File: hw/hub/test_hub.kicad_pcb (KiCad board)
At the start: 2 copper layers, 88.9 x 76.2 mm, 108 parts, among them J1 ARM-SWD, P1 USB_OTG, P2 5V_SEL, P3 5V_EXT, P4 USB1, P5 USB2, P6 USB3, P7 UART, SW1 RST, SW2 BOOT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

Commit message: Update test_hub
No more rescued components
Ripped up all traces
Starting layout again
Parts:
- removed P1: USB_OTG, footprints:10118193-0001LF
- removed P4: USB1, footprints:292303-1
- removed P5: USB2, footprints:292303-1
- removed P6: USB3, footprints:292303-1
- removed R17, R20, R23: R_SNS, footprints:LVK12
- removed R18, R21, R24: 0, Resistors_SMD:R_0603
- removed R19, R22: 100, Resistors_SMD:R_0603
- removed R26, R27, R28: 1k, Resistors_SMD:R_0603
- removed U7, U8, U9: LT6106, footprints:TSOT-23-5
- added C35: 0.1uF, Capacitors_SMD:C_0603, F.Cu at (96.8, 186.3)
- added FB10: Ferrite_Bead, Resistors_SMD:R_0603, F.Cu at (182.0, 146.0)
- added FB7: Ferrite_Bead, Resistors_SMD:R_0603, F.Cu at (188.8, 118.9)
- added FB8: Ferrite_Bead, Resistors_SMD:R_0603, F.Cu at (188.6, 125.9)
- added FB9: Ferrite_Bead, Resistors_SMD:R_0603, F.Cu at (181.6, 138.8)
- added J2: USB_OTG, footprints:USB_MICRO_B, F.Cu at (54.7, 162.8)
- added J3: USB_OTG, footprints:USB_MICRO_B, F.Cu at (52.3, 139.9)
- added J4: USB_A, footprints:292303-1, F.Cu at (178.5, 160.4)
- added J5: USB_A, footprints:292303-1, F.Cu at (193.9, 122.3)
- added J6: USB_A, footprints:292303-1, F.Cu at (189.2, 141.9)
- D6: value LED2 -> LED3
- D7: value LED1 -> LED2
- D8: value LED0 -> LED1
- R16: value 100 -> 330
- moved FB3 103.6 mm to (53.2, 177.0)
- moved FB5 93.2 mm to (55.8, 126.2)
- moved FB4 92.1 mm to (57.4, 157.6)
- moved FB6 91.9 mm to (57.0, 133.4)
- moved C31 81.6 mm to (155.8, 87.0)
- moved D5 81.6 mm to (152.0, 76.9)
- moved R33 81.6 mm to (155.1, 76.9)
- moved U4 81.6 mm to (157.2, 81.4)
- moved C16 81.6 mm to (147.7, 81.6)
- moved C19 81.6 mm to (153.3, 81.4)
- moved C28 81.6 mm to (161.2, 79.0)
- moved R13 81.6 mm to (155.1, 78.9)
- moved U5 59.3 mm to (132.8, 79.8)
- moved C17 59.3 mm to (122.6, 79.7)
- moved C20 59.3 mm to (128.3, 79.8)
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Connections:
- net Net-(R11-Pad1) renamed /ST_USB_N
- net Net-(R12-Pad1) renamed /ST_USB_P
- C28 pad 2: Net-(C28-Pad2) -> /5V_OUT1
- C29 pad 2: Net-(C29-Pad2) -> /5V_OUT2
- C30 pad 2: Net-(C30-Pad2) -> /5V_OUT3
- C31 pad 1: Net-(C28-Pad2) -> /5V_OUT1
- C32 pad 1: Net-(C29-Pad2) -> /5V_OUT2
- C33 pad 1: Net-(C30-Pad2) -> /5V_OUT3
- FB3 pad 1: GND -> Net-(FB3-Pad1)
- FB3 pad 2: Net-(FB3-Pad2) -> +5V
- FB4 pad 1: /5V_OUT2 -> Net-(FB4-Pad1)
- FB4 pad 2: Net-(FB4-Pad2) -> GND
- FB5 pad 1: GND -> +5V
- FB6 pad 1: /5V_OUT3 -> GND
- R16 pad 1: Net-(R16-Pad1) -> GNDPWR
- R16 pad 2: Net-(R16-Pad2) -> GND
- R34 pad 2: /LED2 -> /LED3
- R35 pad 2: /LED1 -> /LED2
- R36 pad 2: /LED0 -> /LED1
- U3 pad 12: /SNS1 -> Net-(U3-Pad12)
- U3 pad 13: /SNS2 -> Net-(U3-Pad13)
- U3 pad 14: /SNS3 -> Net-(U3-Pad14)
- U3 pad 2: /LED0 -> /LED1
- U3 pad 3: /LED1 -> /LED2
- U3 pad 4: /LED2 -> /LED3
- U4 pad 1: Net-(C28-Pad2) -> /5V_OUT1
- U5 pad 1: Net-(C29-Pad2) -> /5V_OUT2
- U6 pad 1: Net-(C30-Pad2) -> /5V_OUT3
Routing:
- net /5V_OUT: track 293.7 -> 0.00 mm, vias 2 -> 0
- net +3V3: track 244.4 -> 0.00 mm, vias 19 -> 0
- net GND: track 218.5 -> 0.00 mm, vias 35 -> 0
- net GNDPWR: track 171.7 -> 0.00 mm, vias 1 -> 0
- net /5V_EN3: track 116.5 -> 0.00 mm, vias 2 -> 0
- net /SNS1: track 112.4 -> 0.00 mm, vias 4 -> 0
- net /5V_FLG3: track 109.3 -> 0.00 mm, vias 2 -> 0
- net /SNS2: track 107.2 -> 0.00 mm, vias 6 -> 0
- net /nRST: track 107.1 -> 0.00 mm, vias 6 -> 0
- net /SNS3: track 105.8 -> 0.00 mm, vias 2 -> 0
- net +5V: track 92.6 -> 0.00 mm, vias 2 -> 0
- net /BOOT0: track 75.9 -> 0.00 mm, vias 6 -> 0
- net /USB3_N: track 69.5 -> 0.00 mm
- net /USB3_P: track 69.3 -> 0.00 mm
- net /5V_FLG1: track 63.5 -> 0.00 mm, vias 2 -> 0
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- removed copper zone on B.Cu, net GND
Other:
- net class Default: clearance 0.16 -> 0.1524; trace_width 0.13 -> 0.1524; via_dia 0.6 -> 0.6858; via_drill 0.305 -> 0.3302
- rule trace_clearance: 0.16 -> 0.1524
- rule trace_min: 0.13 -> 0.1524
- rule via_min_drill: 0.305 -> 0.3302
- rule via_min_size: 0.6 -> 0.6858
- board text added: "USB Test Hub v0.2"
- board text removed: "USB Test Hub v0.1"

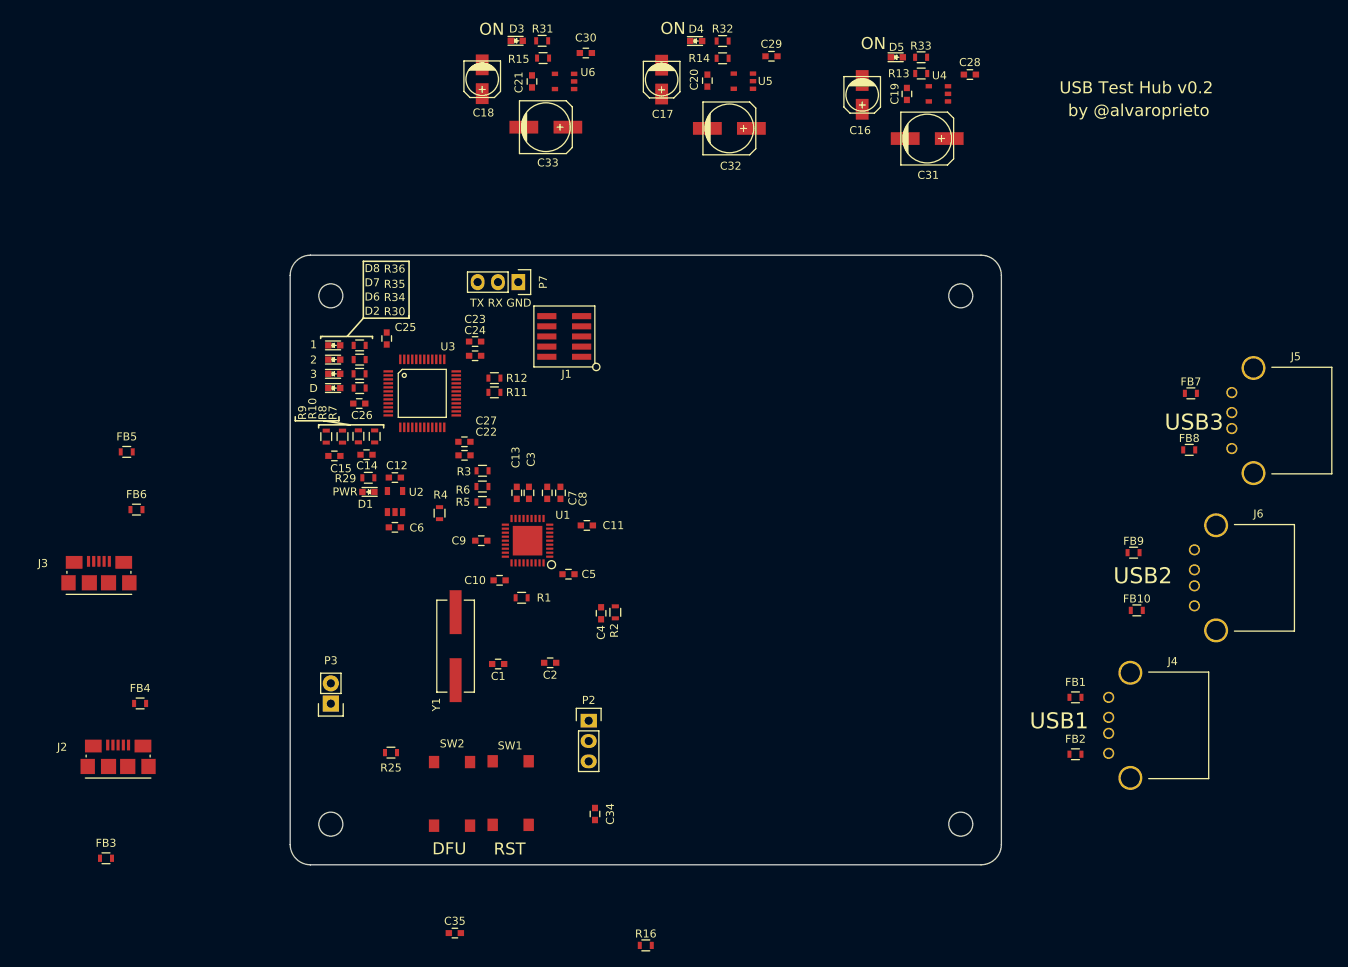
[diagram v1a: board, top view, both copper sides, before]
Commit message: More test_hub work
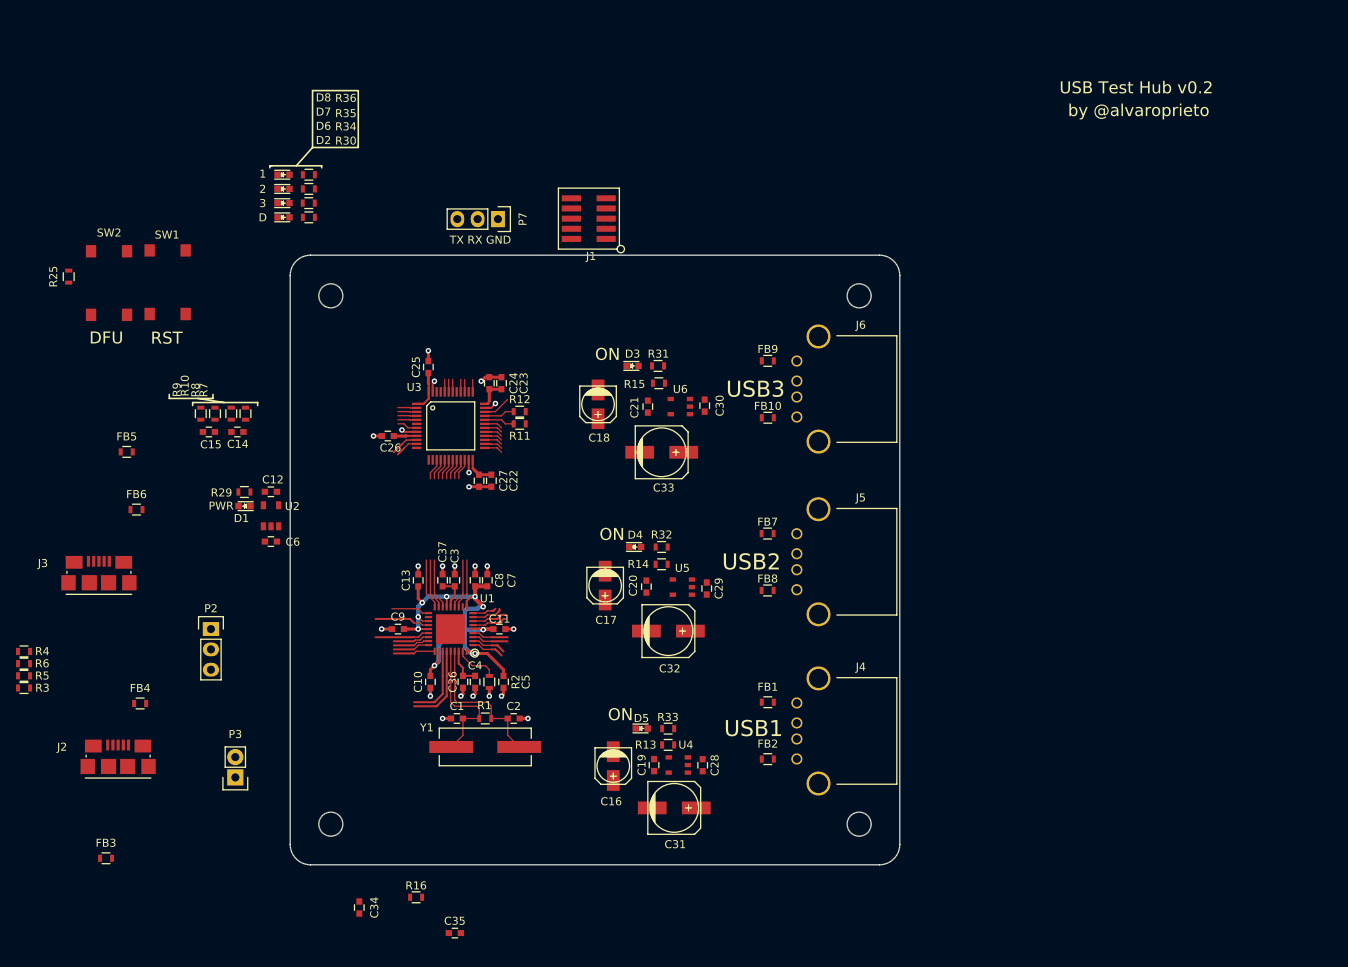
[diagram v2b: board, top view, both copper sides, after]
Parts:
- added C36: 1uF, Capacitors_SMD:C_0603, F.Cu at (97.8, 154.9)
- added C37: 1uF, Capacitors_SMD:C_0603, F.Cu at (95.2, 142.2)
- moved C28 92.6 mm to (127.8, 165.4), turned to 270 degrees
- moved U4 90.0 mm to (124.7, 165.3)
- moved D5 89.8 mm to (120.1, 160.8)
- moved R13 89.7 mm to (123.4, 162.8)
- moved R33 89.7 mm to (123.4, 160.8)
- moved C19 89.7 mm to (121.7, 165.3)
- moved C16 89.5 mm to (116.6, 165.5)
- moved C31 89.4 mm to (124.2, 170.7)
- moved SW1 76.9 mm to (60.9, 105.0)
- moved SW2 76.9 mm to (53.6, 105.1)
- moved R25 71.9 mm to (48.5, 104.3), turned to 90 degrees
- moved C29 67.0 mm to (128.3, 143.3), turned to 270 degrees
- moved U5 63.7 mm to (125.2, 143.1)
- moved C20 63.7 mm to (120.7, 143.0)
- moved D4 63.7 mm to (119.3, 138.1)
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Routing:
- net +3V3: track 0.00 -> 70.1 mm, vias 0 -> 9
- net GND: track 0.00 -> 29.4 mm, vias 0 -> 22
- net Net-(C2-Pad1): track 0.00 -> 18.7 mm
- net Net-(C1-Pad1): track 0.00 -> 17.7 mm
- net /USB_UP_P: track 0.00 -> 10.2 mm
- net /USB_UP_N: track 0.00 -> 9.34 mm
- net /PRTPWR3: track 0.00 -> 8.97 mm
- net /OCS_N2: track 0.00 -> 8.97 mm
- net /PRTPWR2: track 0.00 -> 8.96 mm
- net /OCS_N1: track 0.00 -> 8.95 mm
- net /PRTPWR1: track 0.00 -> 8.95 mm
- net /SDA: track 0.00 -> 8.53 mm
- net /SCL: track 0.00 -> 8.42 mm
- net /VBUS_DET: track 0.00 -> 8.07 mm
- net /OCS_N3: track 0.00 -> 7.50 mm
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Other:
- board size 88.9 x 76.2 mm -> 76.2 x 76.2 mm

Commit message: Continued routing work on test_hub
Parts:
- moved FB3 46.9 mm to (83.3, 141.1)
- moved FB5 41.2 mm to (83.1, 157.1)
- moved FB6 38.3 mm to (83.0, 161.4), turned to 180 degrees
- moved P2 37.6 mm to (100.6, 163.8)
- moved J3 34.2 mm to (80.3, 159.6), turned to 270 degrees
- moved J2 32.2 mm to (80.3, 143.2), turned to 270 degrees
- moved FB4 28.9 mm to (83.3, 144.8)
- moved R3 27.6 mm to (68.2, 144.5)
- moved R4 27.6 mm to (68.2, 140.0)
- moved R5 27.6 mm to (68.2, 143.0)
- moved R6 27.6 mm to (68.2, 141.5)
- moved D2 23.1 mm to (81.7, 119.1)
- moved D7 23.1 mm to (81.7, 115.5)
- moved R30 23.1 mm to (84.9, 119.1)
- moved R35 23.1 mm to (84.9, 115.5)
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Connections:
- FB5 pad 1: +5V -> Net-(FB5-Pad1)
- FB5 pad 2: Net-(FB5-Pad2) -> /5V_EXT
- J3 pad 1: Net-(FB5-Pad2) -> Net-(FB5-Pad1)
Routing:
- net /5V_OUT: track 0.00 -> 192.8 mm, vias 0 -> 3
- net /USB3_N: track 4.40 -> 73.4 mm
- net /USB3_P: track 4.41 -> 73.3 mm
- net GND: track 29.4 -> 86.5 mm, vias 22 -> 37
- net /USB2_N: track 4.55 -> 59.6 mm
- net /USB2_P: track 4.55 -> 59.5 mm
- net /USB1_N: track 4.47 -> 50.2 mm
- net /USB1_P: track 4.36 -> 50.0 mm
- net /USB4_N: track 3.90 -> 35.6 mm
- net /USB4_P: track 3.04 -> 33.8 mm, vias 0 -> 2
- net /5V_EN1: track 2.33 -> 31.9 mm
- net /5V_EN3: track 2.32 -> 31.5 mm
- net /5V_EN2: track 2.33 -> 30.7 mm
- net /5V_FLG3: track 2.31 -> 26.6 mm
- net /5V_FLG1: track 2.32 -> 26.5 mm
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
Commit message: Almost done with test_hub layout
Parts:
- J1, SW1, SW2: moved to B.Cu
- moved SW1 66.9 mm to (127.8, 105.8), turned to 0 degrees
- moved R25 63.2 mm to (111.3, 111.5), turned to 270 degrees
- moved SW2 61.9 mm to (115.4, 105.8), turned to 180 degrees
- moved R5 43.0 mm to (97.8, 111.8), turned to 270 degrees
- moved R6 43.0 mm to (99.3, 111.8), turned to 270 degrees
- moved P7 33.6 mm to (106.9, 130.3)
- moved J1 26.9 mm to (89.7, 109.4), turned to 180 degrees
- moved C34 24.7 mm to (113.3, 173.2)
- moved R3 23.9 mm to (88.9, 132.6), turned to 270 degrees
- moved R4 23.9 mm to (88.9, 128.0), turned to 90 degrees
- moved R16 21.9 mm to (115.2, 173.2)
- moved C35 21.1 mm to (117.1, 173.2)
- moved FB5 1.14 mm to (83.1, 158.2)
- moved FB6 0.38 mm to (83.0, 161.0)
- moved FB4 0.25 mm to (83.3, 144.5)
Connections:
- U3 pad 10: /VBUS_DET -> /VBUS_EXT_DET
- U3 pad 11: /VBUS_EXT_DET -> /SUSP_IND
- U3 pad 12: Net-(U3-Pad12) -> /VBUS_DET
- U3 pad 13: Net-(U3-Pad13) -> /HUB_RST_N
- U3 pad 14: Net-(U3-Pad14) -> /CFG_SEL1
- U3 pad 26: /5V_EN2 -> /5V_FLG1
- U3 pad 27: /5V_EN3 -> /5V_EN2
- U3 pad 28: /HUB_RST_N -> /5V_FLG2
- U3 pad 29: /5V_FLG1 -> /5V_EN3
- U3 pad 30: /5V_FLG2 -> /5V_FLG3
- U3 pad 31: /5V_FLG3 -> Net-(U3-Pad31)
- U3 pad 39: /SUSP_IND -> Net-(U3-Pad39)
- U3 pad 40: /CFG_SEL1 -> Net-(U3-Pad40)
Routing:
- net /5V_EN1: track 31.9 -> 158.7 mm, vias 0 -> 2
- net GNDPWR: track 0.00 -> 123.4 mm
- net /5V_FLG1: track 26.5 -> 149.8 mm, vias 0 -> 2
- net /5V_EN2: track 30.7 -> 127.2 mm, vias 0 -> 2
- net +3V3: track 70.1 -> 165.5 mm, vias 9 -> 17
- net /5V_FLG2: track 25.8 -> 119.0 mm, vias 0 -> 2
- net +5V: track 0.00 -> 66.8 mm, vias 0 -> 2
- net /5V_EN3: track 31.5 -> 95.2 mm, vias 0 -> 2
- net /5V_FLG3: track 26.6 -> 87.9 mm, vias 0 -> 2
- net /nRST: track 2.56 -> 63.2 mm, vias 0 -> 4
- net /VBUS_DET: track 8.07 -> 43.6 mm, vias 0 -> 2
- net /SCL: track 8.42 -> 43.5 mm, vias 0 -> 2
- net /HUB_RST_N: track 4.56 -> 34.7 mm, vias 0 -> 2
- net /SUSP_IND: track 6.79 -> 34.7 mm
- net /CFG_SEL1: track 6.13 -> 33.7 mm, vias 0 -> 2
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- added copper zone on B.Cu, net GND

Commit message: All connections made!
Now I just need to fix the USB clearances...
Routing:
- net /5V_OUT: track 209.3 -> 271.8 mm, vias 3 -> 5
- net /BOOT0: track 12.3 -> 34.2 mm, vias 1 -> 5
- net +3V3: track 165.5 -> 185.5 mm, vias 17 -> 19
- net GND: track 107.3 -> 115.1 mm, vias 43 -> 46

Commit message: Layout done!
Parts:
- moved J6 0.06 mm to (139.5, 118.3)
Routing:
- net GNDPWR: track 123.4 -> 162.9 mm
- net /USB4_N: track 35.6 -> 30.2 mm, vias 0 -> 2
- net /USB4_P: track 33.8 -> 30.2 mm, vias 2 -> 0
- net /USB3_N: track 73.4 -> 70.5 mm
- net /USB3_P: track 73.3 -> 70.4 mm
- net /USB_UP_N: track 26.2 -> 28.1 mm
- net /USB_UP_P: track 27.1 -> 28.1 mm
- net /USB1_N: track 50.2 -> 49.1 mm
- net /USB1_P: track 50.0 -> 49.1 mm
- net /USB2_N: track 59.6 -> 59.0 mm
